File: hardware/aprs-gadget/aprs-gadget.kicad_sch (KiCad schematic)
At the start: 27 parts

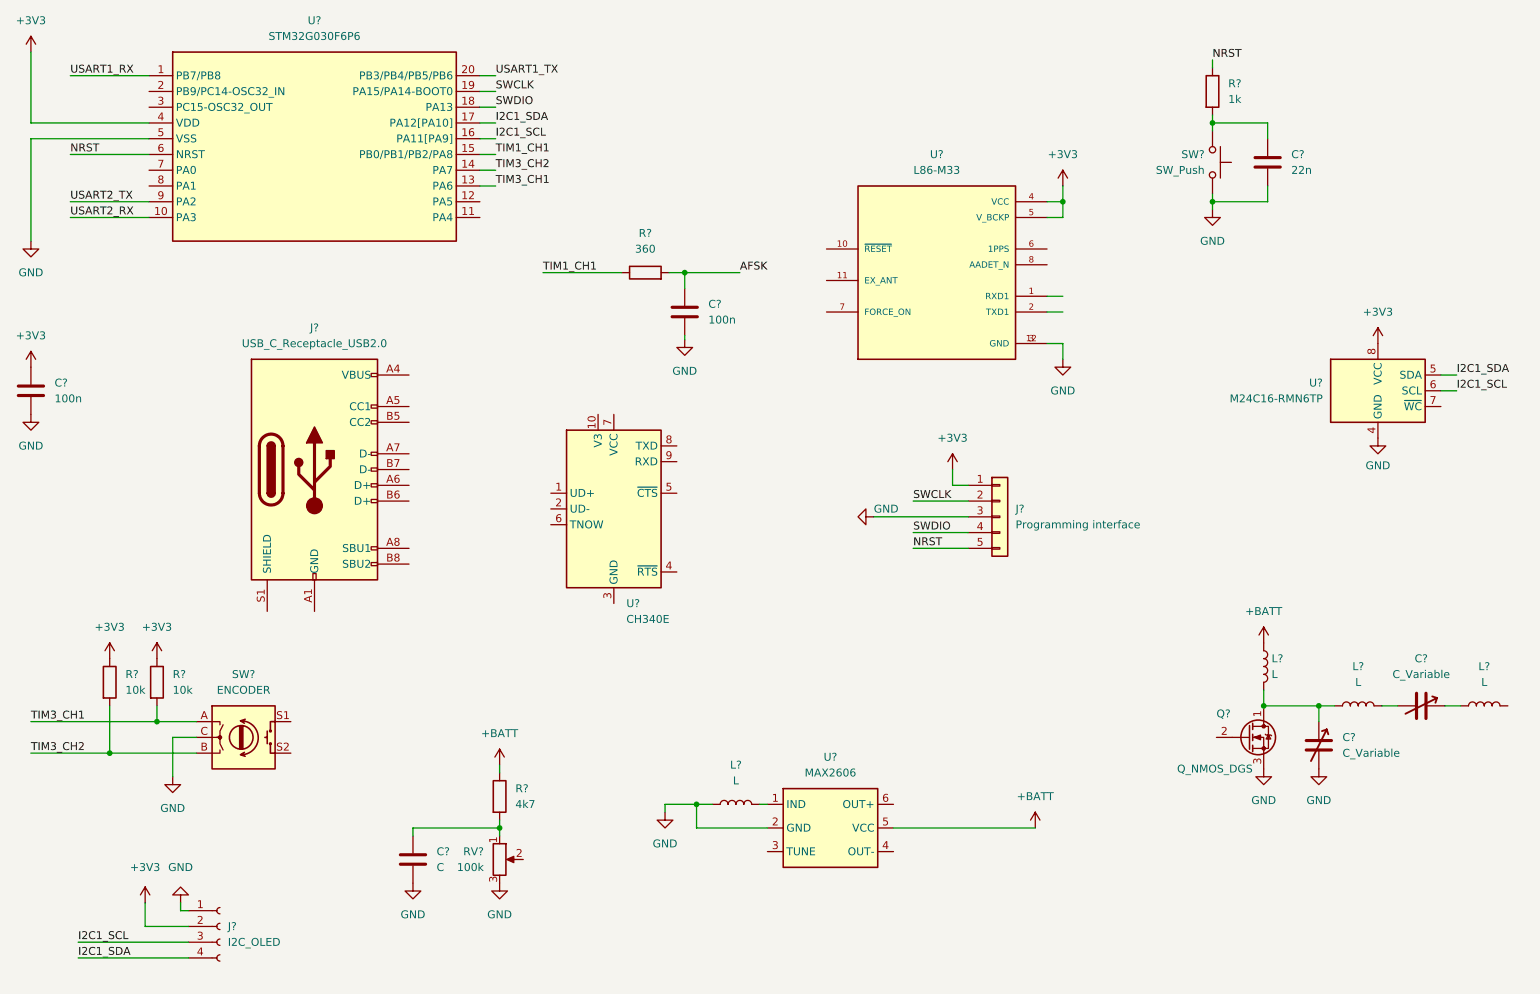
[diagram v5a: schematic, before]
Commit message: Replace GNSS and add DRA818V module
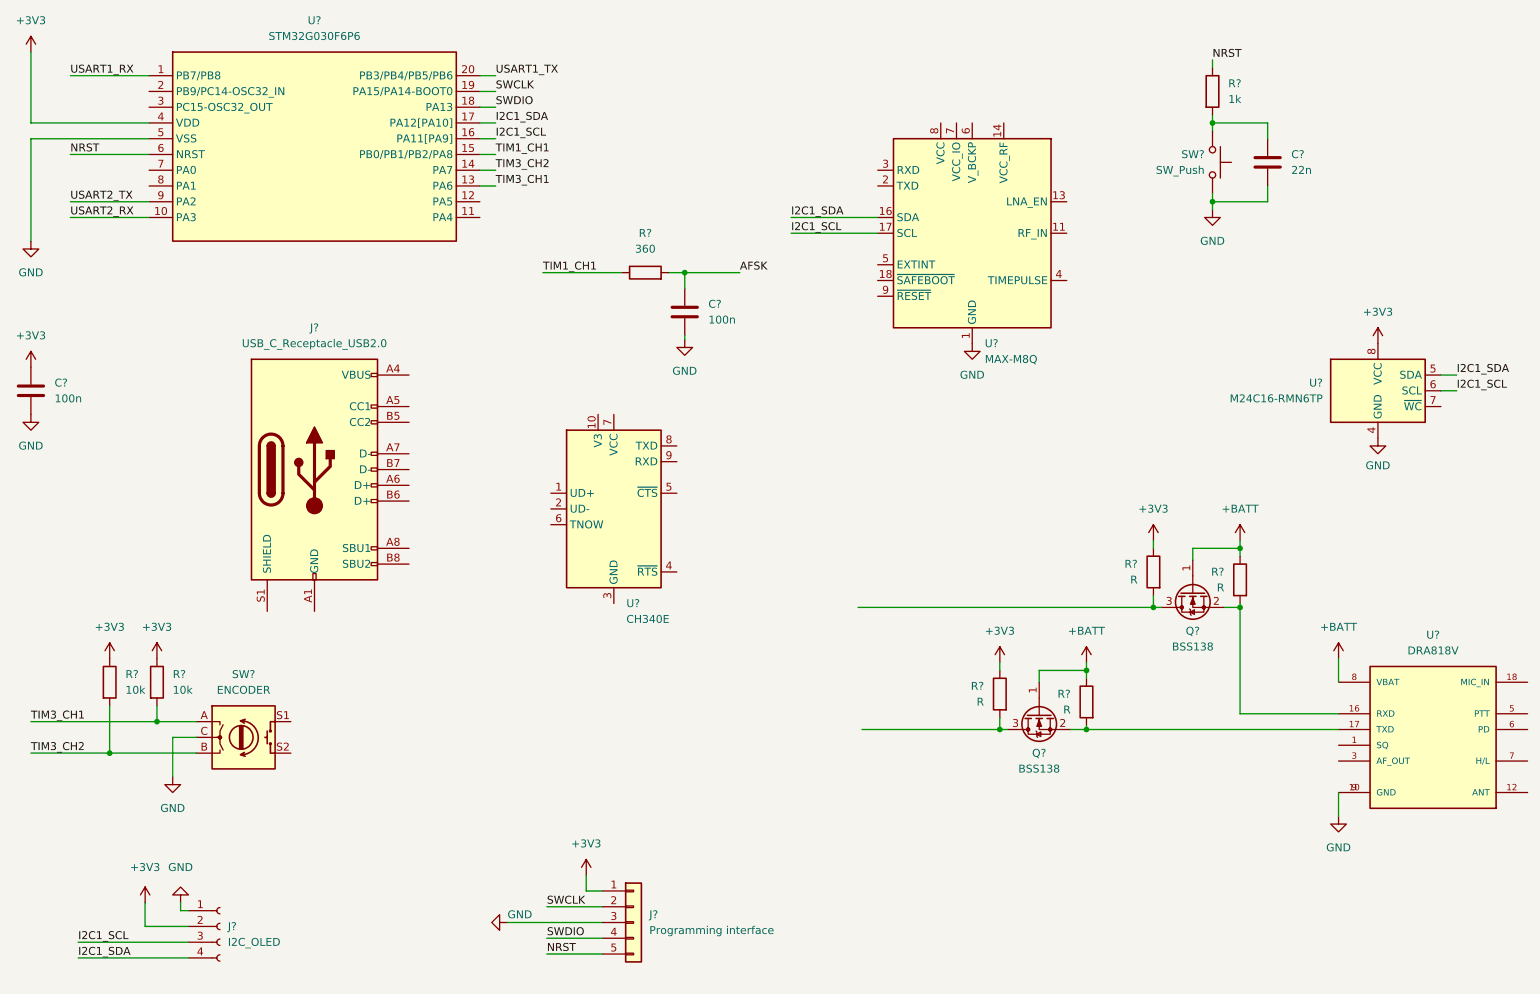
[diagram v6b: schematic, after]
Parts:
- removed C? (x2): C_Variable, symbol Device:C_Variable
- removed C?: C, symbol Device:C
- removed L? (x4): L, symbol Device:L
- removed Q?: Q_NMOS_DGS, symbol Device:Q_NMOS_DGS
- removed R?: 4k7, symbol Device:R
- removed RV?: 100k, symbol Device:R_Potentiometer
- removed U?: L86-M33, XCVR_L86-M33, symbol L86-M33:L86-M33
- removed U?: MAX2606, symbol MAX2606:MAX2606
- added Q? (x2): BSS138, Package_TO_SOT_SMD:SOT-23, symbol Transistor_FET:BSS138
- added R? (x4): R, symbol Device:R
- added U?: DRA818V, DORJI_DRA818V, symbol DRA818V:DRA818V
- added U?: MAX-M8Q, RF_GPS:ublox_MAX, symbol RF_GPS:MAX-M8Q
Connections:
- net +3V3: now also R?.1, R?.1
- net +BATT: now also Q?.1 (G), Q?.1 (G), R?.1, R?.1, U?.8 (VBAT)
- net GND: now also U?.1 (GND), U?.10 (GND), U?.10 (GND), U?.12 (GND), U?.9 (GND)
- net I2C1_SCL: now also U?.17 (SCL)
- net I2C1_SDA: now also U?.16 (SDA)
- new net: Q?.2 (S), R?.2, U?.16 (RXD)
- new net: Q?.2 (S), R?.2, U?.17 (TXD)
- new net: Q?.3 (D), R?.2 (x2)
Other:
- moved on the sheet: J?

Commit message: Make schematic more structured, add Goertzel-filter based afsk deconder
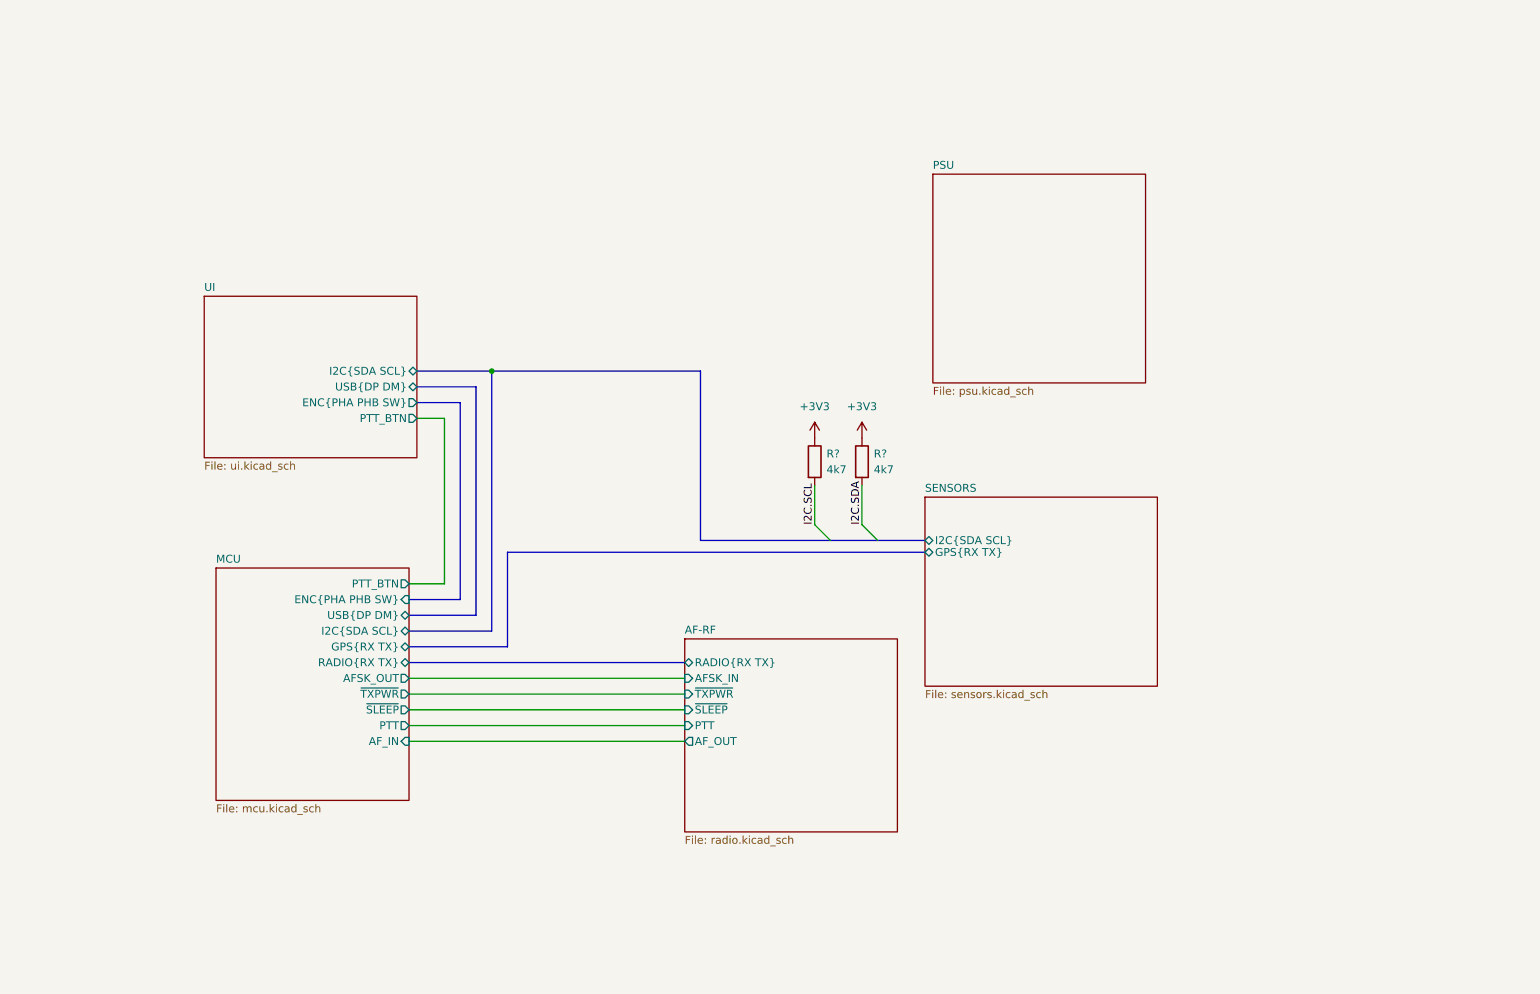
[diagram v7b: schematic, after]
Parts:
- removed C? (x2): 100n, symbol Device:C
- removed C?: 22n, symbol Device:C
- removed J?: I2C_OLED, symbol Connector:Conn_01x04_Female
- removed J?: USB_C_Receptacle_USB2.0, Connector_USB:USB_C_Receptacle_GCT_USB4085, symbol Connector:USB_C_Receptacle_USB2.0
- removed J?: Programming interface, symbol Connector_Generic:Conn_01x05
- removed Q? (x2): BSS138, Package_TO_SOT_SMD:SOT-23, symbol Transistor_FET:BSS138
- removed R? (x2): 10k, symbol Device:R
- removed R?: 1k, symbol Device:R
- removed R? (x4): R, symbol Device:R
- removed R?: 360, symbol Device:R
- removed SW?: ENCODER, symbol Device:RotaryEncoder_Switch
- removed SW?: SW_Push, symbol Switch:SW_Push
- removed U?: STM32G030F6P6, Package_SO:TSSOP-20_4.4x6.5mm_P0.65mm, symbol STM32G030:STM32G030F6P6
- removed U?: DRA818V, DORJI_DRA818V, symbol DRA818V:DRA818V
- removed U?: M24C16-RMN6TP, Package_SO:SOIC-8_3.9x4.9mm_P1.27mm, symbol Memory_EEPROM:AT24CS16-SSHM
- removed U?: MAX-M8Q, RF_GPS:ublox_MAX, symbol RF_GPS:MAX-M8Q
- removed U?: CH340E, Package_SO:MSOP-10_3x3mm_P0.5mm, symbol Interface_USB:CH340E
- added R? (x2): 4k7, symbol Device:R
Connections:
- net +3V3: now also R?.1, R?.1
- new net I2C.SCL: R?.2
- new net I2C.SDA: R?.2
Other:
- added sheet AF-RF (radio.kicad_sch)
- added sheet MCU (mcu.kicad_sch)
- added sheet PSU (psu.kicad_sch)
- added sheet SENSORS (sensors.kicad_sch)
- added sheet UI (ui.kicad_sch)
